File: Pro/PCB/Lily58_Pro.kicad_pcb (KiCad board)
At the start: 2 copper layers, 137.5 x 109.5 mm, 85 parts, among them J1 LED, J2 4PIN, J3 OLED, P1 i2c_pin, P2 i2c_pin, SW1 SW_PUSH, SW10 SW_PUSH, SW11 SW_PUSH, SW12 SW_PUSH, SW13 SW_PUSH, SW14 SW_PUSH, SW15 SW_PUSH, SW16 SW_PUSH, SW17 SW_PUSH, SW18 SW_PUSH, SW19 SW_PUSH, SW2 SW_PUSH, SW20 SW_PUSH, SW21 SW_PUSH, SW22 SW_PUSH, SW23 SW_PUSH, SW24 SW_PUSH, SW25 Rotary_Encoder_Switch, SW26 SW_PUSH, SW27 SW_PUSH, SW28 SW_PUSH, SW29 SW_PUSH, SW3 SW_PUSH, SW30 SW_PUSH, SW4 SW_PUSH, SW5 SW_PUSH, SW6 SW_PUSH, SW7 SW_PUSH, SW8 SW_PUSH, SW9 SW_PUSH, U1 ProMicro

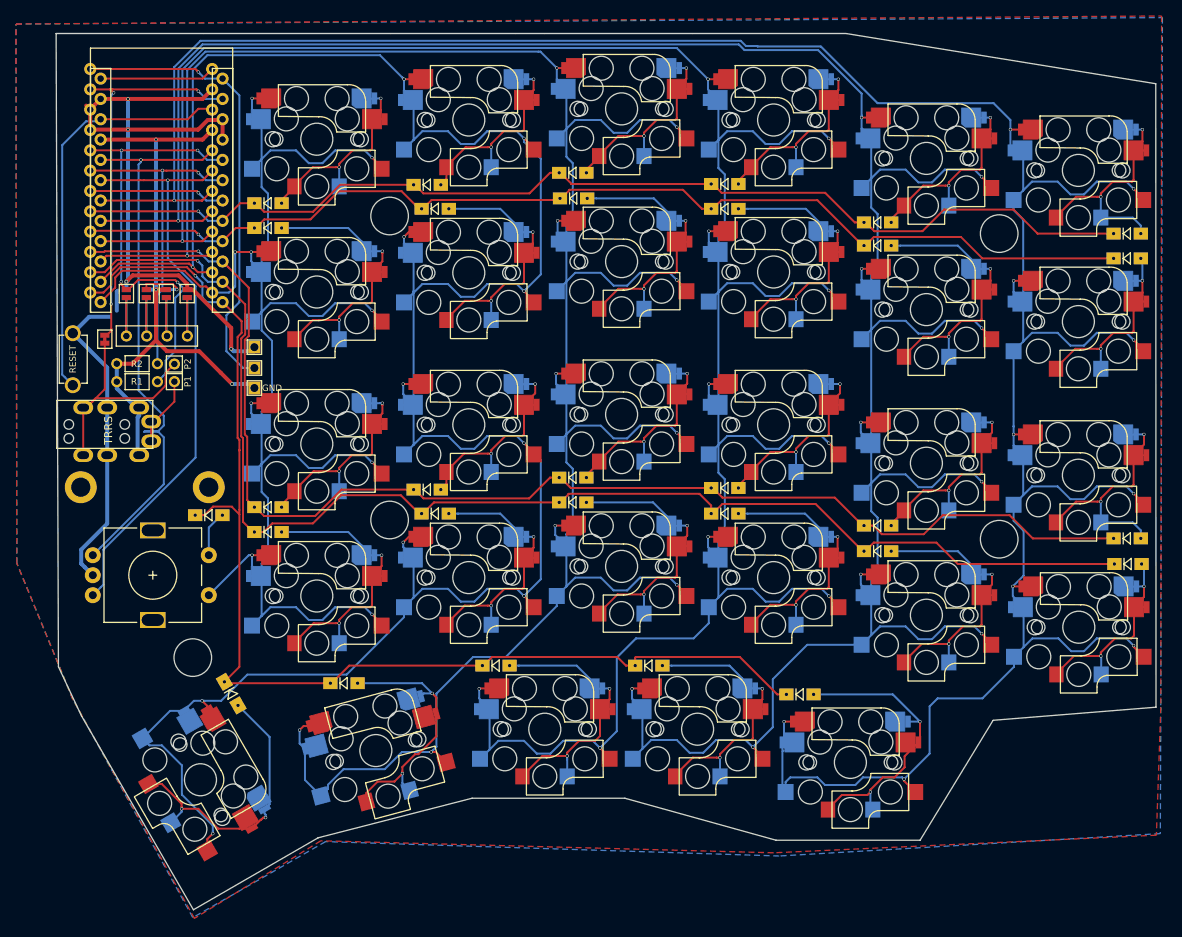
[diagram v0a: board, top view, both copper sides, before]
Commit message: Better edge shape, copper pour vias, better drill holes
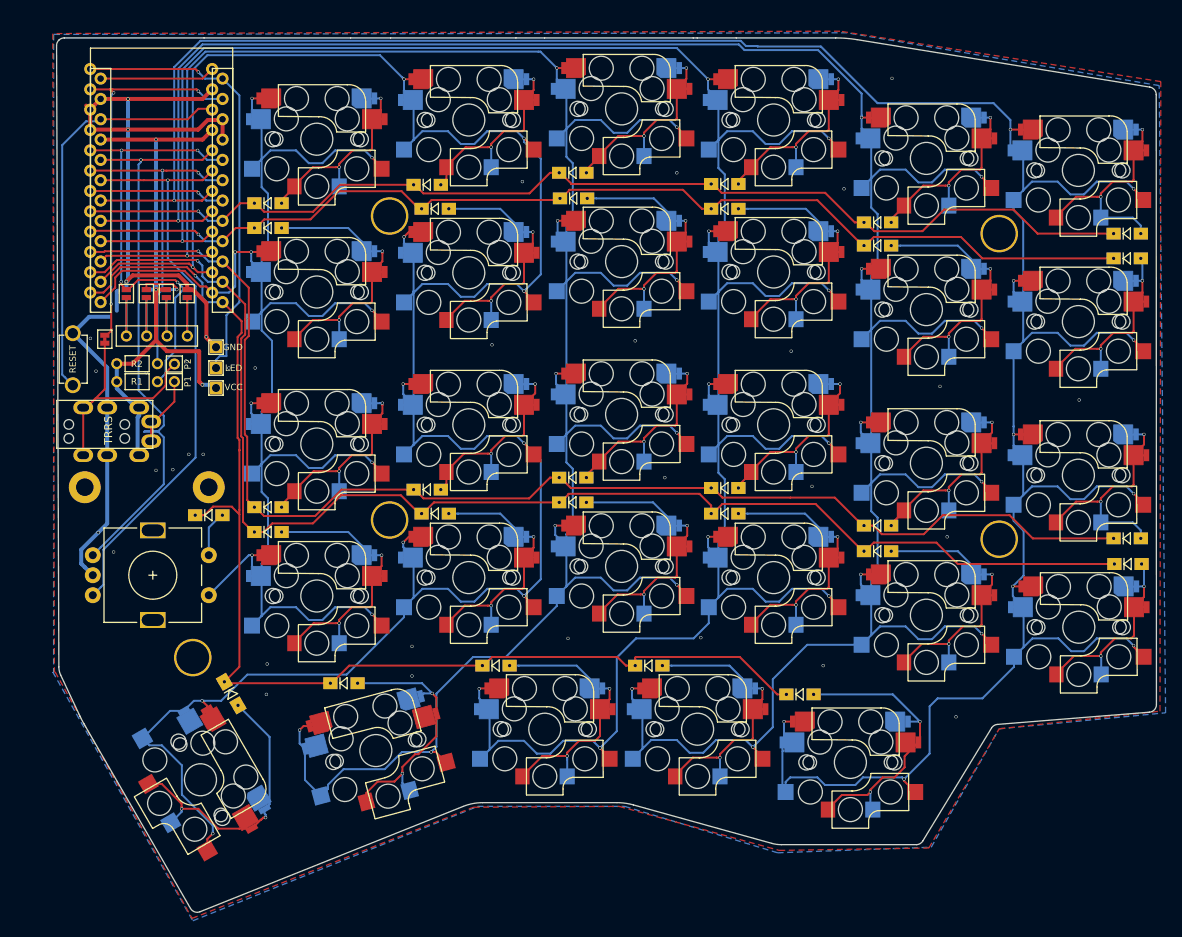
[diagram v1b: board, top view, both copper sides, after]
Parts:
- moved J1 4.80 mm to (107.9, 81.1)
- moved TH1 0.50 mm to (91.5, 93.5)
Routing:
- net GND: track 128.0 -> 124.4 mm, vias 4 -> 36
- net VCC: track 76.5 -> 74.2 mm
- net LED: track 57.0 -> 55.8 mm
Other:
- board size 137.5 x 109.5 mm -> 137.5 x 109.3 mm
